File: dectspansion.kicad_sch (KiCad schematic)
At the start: 24 parts, among them J1 Hexpansion-Connector, J2 Conn_01x03_Pin, J3 AudioJack4, J4 Conn_01x02_Pin, U1 SC14CVMDECT, U3 24LC00

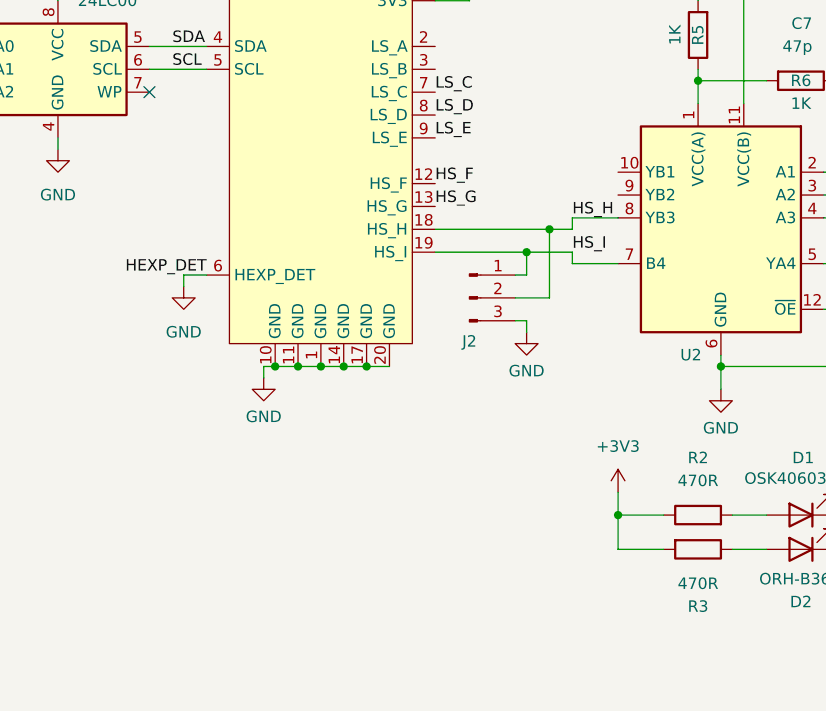
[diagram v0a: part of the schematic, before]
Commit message: Added piezo ringer
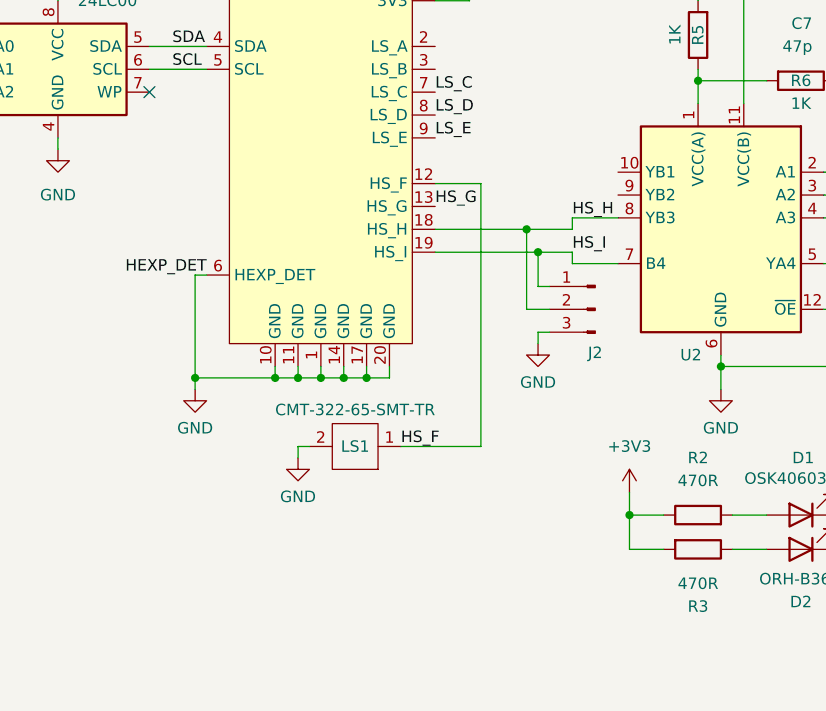
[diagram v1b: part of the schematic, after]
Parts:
- added LS1: CMT-322-65-SMT-TR, micro_piezo:CMT-322-65-SMT-TR, symbol CMT-322-65-SMT-TR:CMT-322-65-SMT-TR
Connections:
- net GND: now also LS1.2
- net HS_F: now also LS1.1
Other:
- moved on the sheet: J2
